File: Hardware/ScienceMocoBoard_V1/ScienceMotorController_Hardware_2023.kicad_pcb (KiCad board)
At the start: 2 copper layers, 153 x 106.4 mm, 189 parts, among them J1 RJ45_LED_Shielded, J2 Conn_02x03_Counter_Clockwise, Q1 SI4156DY, Q10 SI4156DY, Q11 SI4156DY, Q12 SI4156DY, Q13 SI4156DY, Q14 SI4156DY, Q15 SI4156DY, Q16 SI4156DY, Q2 SI4156DY, Q3 SI4156DY, Q4 SI4156DY, Q5 SI4156DY, Q6 SI4156DY, Q7 SI4156DY, Q8 SI4156DY, Q9 SI4156DY, SW1 SW_Push, SW10 SW_Push, SW11 SW_DPDT_x2, SW2 SW_Push, SW3 SW_Push, SW4 SW_Push, SW5 SW_Push, SW6 SW_Push, SW7 SW_Push, SW8 SW_Push, SW9 SW_Push, U1 74LVC2G04, U10 IRS2005S, U11 Teensy4.1_DEV-16771, U12 74LVC2G04, U13 IRS2005S, U14 IRS2005S, U15 IRS2005S, U2 IRS2005S, U3 3V3 OKI, U4 TSR_1-2450, U5 74LVC2G04, U6 IRS2005S, U7 IRS2005S, U8 IRS2005S, U9 74LVC2G04

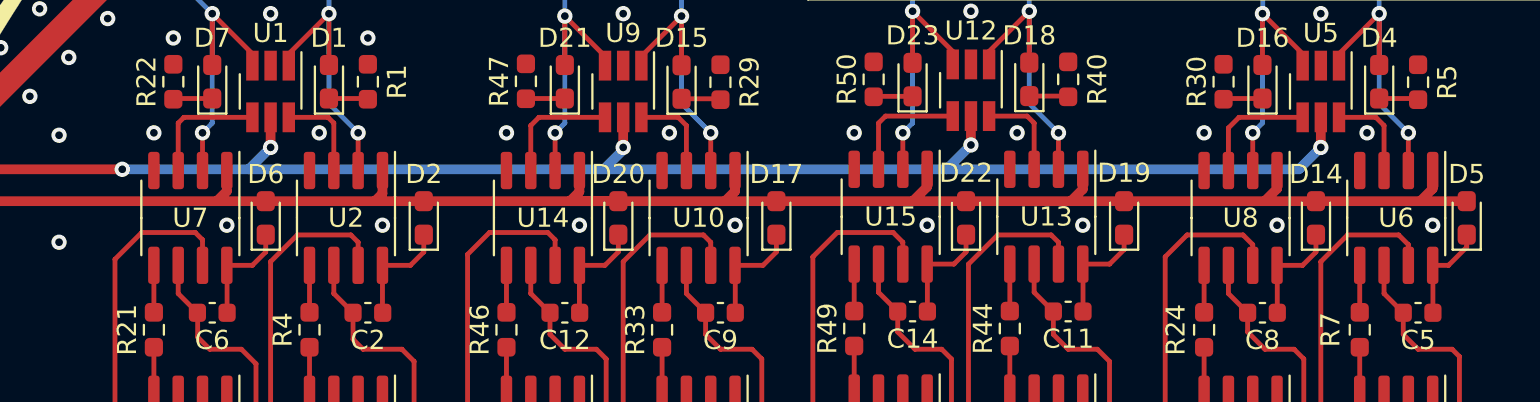
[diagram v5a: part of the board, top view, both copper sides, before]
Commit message: Fixed trace + made STEP file
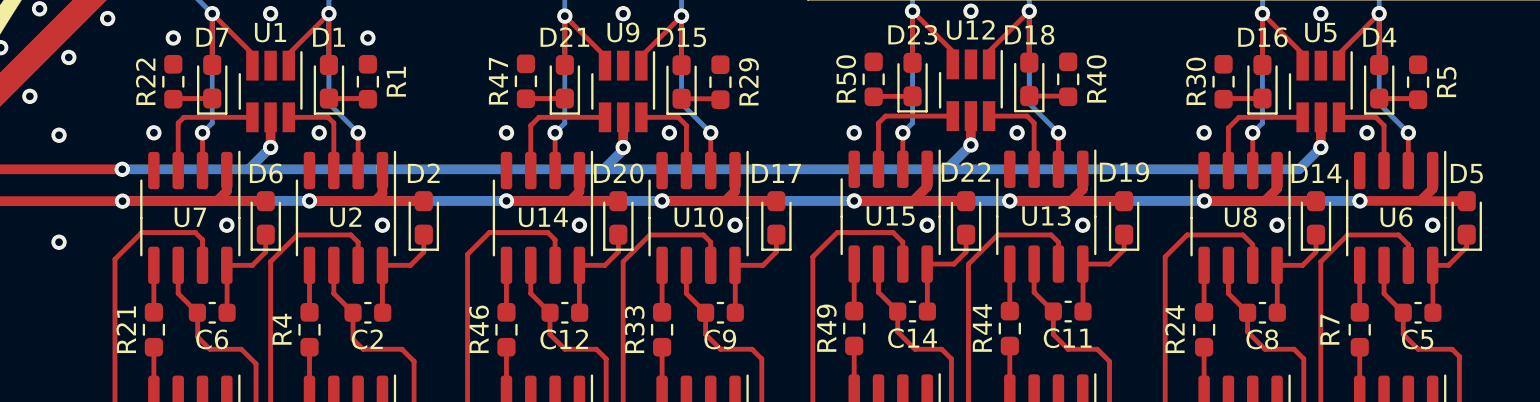
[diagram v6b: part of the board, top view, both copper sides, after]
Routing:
- net +12V: track 137.6 -> 178.1 mm, vias 69 -> 77
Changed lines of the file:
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@@
   (segment (start 123.4955 71.88) (end 66.294 71.88) (width 0.254) (layer "F.Cu") (net 6))
   (segment (start 64.90875 75.81795) (end 64.90875 78.7558) (width 0.254) (layer "F.Cu") (net 6))
+  (segment (start 145.175 117.235) (end 145.161 117.221) (width 0.508) (layer "F.Cu") (net 7))
+  (segment (start 130.288 117.235) (end 127.014 117.235) (width 0.508) (layer "F.Cu") (net 7))
   (segment (start 159.118 115.635) (end 159.118 116.586) (width 0.508) (layer "F.Cu") (net 7))
-  (segment (start 124.714 117.235) (end 130.288 117.235) (width 0.508) (layer "F.Cu") (net 7))
+  (segment (start 127.014 117.235) (end 127 117.221) (width 0.508) (layer "F.Cu") (net 7))
+  (segment (start 140.095 117.235) (end 137.047 117.235) (width 0.508) (layer "F.Cu") (net 7))
+  (segment (start 88.505 117.235) (end 84.328 121.412) (width 0.508) (layer "F.Cu") (net 7))
+  (segment (start 148.35 117.235) (end 145.175 117.235) (width 0.508) (layer "F.Cu") (net 7))
   (segment (start 148.971 115.57) (end 148.971 116.614) (width 0.508) (layer "F.Cu") (net 7))
   (segment (start 112.395 115.635) (end 112.395 116.84) (width 0.508) (layer "F.Cu") (net 7))
   (segment (start 42.6865 111.01575) (end 48.38375 116.713) (width 0.254) (layer "F.Cu") (net 7))
   (segment (start 158.469 117.235) (end 161.15 117.235) (width 0.508) (layer "F.Cu") (net 7))
-  (segment (start 151.13 117.235) (end 158.469 117.235) (width 0.508) (layer "F.Cu") (net 7))
-  (segment (start 84.328 121.412) (end 84.328 136.4628) (width 0.508) (layer "F.Cu") (net 7))
-  (segment (start 103.745 117.235) (end 88.505 117.235) (width 0.508) (layer "F.Cu") (net 7))
-  (segment (start 88.505 117.235) (end 84.328 121.412) (width 0.508) (layer "F.Cu") (net 7))
+  (segment (start 122.188 117.235) (end 118.886 117.235) (width 0.508) (layer "F.Cu") (net 7))
   (segment (start 48.387 123.19) (end 48.387 127.508) (width 0.254) (layer "F.Cu") (net 7))
   (segment (start 166.597 117.235) (end 169.024 117.235) (width 0.508) (layer "F.Cu") (net 7))
+  (segment (start 158.455 117.221) (end 158.469 117.235) (width 0.508) (layer "F.Cu") (net 7))
   (segment (start 104.267 116.713) (end 103.745 117.235) (width 0.508) (layer "F.Cu") (net 7))
   (segment (start 42.6865 111.01575) (end 42.6865 111.001) (width 0.254) (layer "F.Cu") (net 7))
+  (segment (start 84.328 121.412) (end 84.328 136.4628) (width 0.508) (layer "F.Cu") (net 7))
   (segment (start 159.118 116.586) (end 158.469 117.235) (width 0.508) (layer "F.Cu") (net 7))
   (segment (start 148.971 116.614) (end 148.35 117.235) (width 0.508) (layer "F.Cu") (net 7))
+  (segment (start 103.745 117.235) (end 88.505 117.235) (width 0.508) (layer "F.Cu") (net 7))
   (segment (start 140.843 115.57) (end 140.843 116.487) (width 0.508) (layer "F.Cu") (net 7))
   (segment (start 122.682 116.741) (end 122.188 117.235) (width 0.508) (layer "F.Cu") (net 7))
+  (segment (start 155.321 117.221) (end 158.455 117.221) (width 0.508) (layer "F.Cu") (net 7))
   (segment (start 140.095 117.235) (end 142.875 117.235) (width 0.508) (layer "F.Cu") (net 7))
-  (segment (start 142.875 117.235) (end 148.35 117.235) (width 0.508) (layer "F.Cu") (net 7))
+  (segment (start 112 117.235) (end 111.986 117.221) (width 0.508) (layer "F.Cu") (net 7))
   (segment (start 167.246 115.635) (end 167.246 116.586) (width 0.508) (layer "F.Cu") (net 7))
   (segment (start 167.246 116.586) (end 166.597 117.235) (width 0.508) (layer "F.Cu") (net 7))
-  (segment (start 132.969 117.235) (end 140.095 117.235) (width 0.508) (layer "F.Cu") (net 7))
-  (segment (start 114.554 117.235) (end 124.601 117.235) (width 0.508) (layer "F.Cu") (net 7))
+  (segment (start 111.986 117.221) (end 108.585 117.221) (width 0.508) (layer "F.Cu") (net 7))
+  (segment (start 137.047 117.235) (end 137.033 117.221) (width 0.508) (layer "F.Cu") (net 7))
   (segment (start 130.288 117.235) (end 132.969 117.235) (width 0.508) (layer "F.Cu") (net 7))
+  (segment (start 166.583 117.221) (end 166.597 117.235) (width 0.508) (layer "F.Cu") (net 7))
   (segment (start 112.395 116.84) (end 112 117.235) (width 0.508) (layer "F.Cu") (net 7))
   (segment (start 130.81 115.635) (end 130.81 116.713) (width 0.508) (layer "F.Cu") (net 7))
   (segment (start 48.38375 116.713) (end 48.387 116.713) (width 0.254) (layer "F.Cu") (net 7))
-  (segment (start 161.15 117.235) (end 166.597 117.235) (width 0.508) (layer "F.Cu") (net 7))
+  (segment (start 163.449 117.221) (end 166.583 117.221) (width 0.508) (layer "F.Cu") (net 7))
   (segment (start 130.81 116.713) (end 130.288 117.235) (width 0.508) (layer "F.Cu") (net 7))
-  (segment (start 106.299 117.235) (end 112 117.235) (width 0.508) (layer "F.Cu") (net 7))
   (segment (start 148.35 117.235) (end 151.13 117.235) (width 0.508) (layer "F.Cu") (net 7))
   (segment (start 103.745 117.235) (end 106.299 117.235) (width 0.508) (layer "F.Cu") (net 7))
@@
   (segment (start 112 117.235) (end 114.554 117.235) (width 0.508) (layer "F.Cu") (net 7))
   (segment (start 140.843 116.487) (end 140.095 117.235) (width 0.508) (layer "F.Cu") (net 7))
+  (segment (start 118.886 117.235) (end 118.872 117.221) (width 0.508) (layer "F.Cu") (net 7))
   (segment (start 122.682 115.635) (end 122.682 116.741) (width 0.508) (layer "F.Cu") (net 7))
   (segment (start 122.188 117.235) (end 124.714 117.235) (width 0.508) (layer "F.Cu") (net 7))
@@
   (via (at 143.002 148.336) (size 0.8) (drill 0.4) (layers "F.Cu" "B.Cu") (free) (net 7))
   (via (at 69.977 148.209) (size 0.8) (drill 0.4) (layers "F.Cu" "B.Cu") (free) (net 7))
+  (via (at 98.82 117.235) (size 0.8) (drill 0.4) (layers "F.Cu" "B.Cu") (net 7))
   (via (at 112.395 148.59) (size 0.8) (drill 0.4) (layers "F.Cu" "B.Cu") (free) (net 7))
   (via (at 161.29 148.336) (size 0.8) (drill 0.4) (layers "F.Cu" "B.Cu") (free) (net 7))
@@
   (via (at 111.125 148.59) (size 0.8) (drill 0.4) (layers "F.Cu" "B.Cu") (free) (net 7))
   (via (at 122.682 148.336) (size 0.8) (drill 0.4) (layers "F.Cu" "B.Cu") (free) (net 7))
+  (via (at 137.033 117.221) (size 0.8) (drill 0.4) (layers "F.Cu" "B.Cu") (net 7))
   (via (at 51.689 154.178) (size 0.8) (drill 0.4) (layers "F.Cu" "B.Cu") (free) (net 7))
   (via (at 143.002 156.464) (size 0.8) (drill 0.4) (layers "F.Cu" "B.Cu") (free) (net 7))
@@
   (via (at 104.267 148.59) (size 0.8) (drill 0.4) (layers "F.Cu" "B.Cu") (free) (net 7))
   (via (at 69.977 154.305) (size 0.8) (drill 0.4) (layers "F.Cu" "B.Cu") (free) (net 7))
+  (via (at 108.585 117.221) (size 0.8) (drill 0.4) (layers "F.Cu" "B.Cu") (net 7))
   (via (at 143.002 152.4) (size 0.8) (drill 0.4) (layers "F.Cu" "B.Cu") (free) (net 7))
   (via (at 164.706 148.463) (size 0.8) (drill 0.4) (layers "F.Cu" "B.Cu") (free) (net 7))
@@
   (via (at 124.714 148.336) (size 0.8) (drill 0.4) (layers "F.Cu" "B.Cu") (free) (net 7))
   (via (at 48.387 116.713) (size 0.8) (drill 0.4) (layers "F.Cu" "B.Cu") (net 7))
+  (via (at 155.321 117.221) (size 0.8) (drill 0.4) (layers "F.Cu" "B.Cu") (net 7))
   (via (at 143.002 154.432) (size 0.8) (drill 0.4) (layers "F.Cu" "B.Cu") (free) (net 7))
   (via (at 88.265 154.432) (size 0.8) (drill 0.4) (layers "F.Cu" "B.Cu") (free) (net 7))
@@
   (via (at 124.714 152.4) (size 0.8) (drill 0.4) (layers "F.Cu" "B.Cu") (free) (net 7))
   (via (at 109.855 148.59) (size 0.8) (drill 0.4) (layers "F.Cu" "B.Cu") (free) (net 7))
+  (via (at 163.449 117.221) (size 0.8) (drill 0.4) (layers "F.Cu" "B.Cu") (net 7))
   (via (at 101.727 148.59) (size 0.8) (drill 0.4) (layers "F.Cu" "B.Cu") (free) (net 7))
   (via (at 69.977 150.241) (size 0.8) (drill 0.4) (layers "F.Cu" "B.Cu") (free) (net 7))
@@
   (via (at 102.997 148.59) (size 0.8) (drill 0.4) (layers "F.Cu" "B.Cu") (free) (net 7))
   (via (at 129.54 148.336) (size 0.8) (drill 0.4) (layers "F.Cu" "B.Cu") (free) (net 7))
+  (via (at 118.872 117.221) (size 0.8) (drill 0.4) (layers "F.Cu" "B.Cu") (net 7))
   (via (at 140.843 148.463) (size 0.8) (drill 0.4) (layers "F.Cu" "B.Cu") (free) (net 7))
   (via (at 145.161 148.463) (size 0.8) (drill 0.4) (layers "F.Cu" "B.Cu") (free) (net 7))
   (via (at 88.265 156.464) (size 0.8) (drill 0.4) (layers "F.Cu" "B.Cu") (free) (net 7))
+  (via (at 127 117.221) (size 0.8) (drill 0.4) (layers "F.Cu" "B.Cu") (net 7))
   (via (at 69.977 156.337) (size 0.8) (drill 0.4) (layers "F.Cu" "B.Cu") (free) (net 7))
   (via (at 161.29 152.4) (size 0.8) (drill 0.4) (layers "F.Cu" "B.Cu") (free) (net 7))
@@
   (via (at 88.265 150.368) (size 0.8) (drill 0.4) (layers "F.Cu" "B.Cu") (free) (net 7))
   (via (at 106.426 152.654) (size 0.8) (drill 0.4) (layers "F.Cu" "B.Cu") (free) (net 7))
+  (via (at 145.161 117.221) (size 0.8) (drill 0.4) (layers "F.Cu" "B.Cu") (net 7))
   (via (at 51.689 148.082) (size 0.8) (drill 0.4) (layers "F.Cu" "B.Cu") (free) (net 7))
   (via (at 88.265 152.4) (size 0.8) (drill 0.4) (layers "F.Cu" "B.Cu") (free) (net 7))
   (via (at 157.848 148.463) (size 0.8) (drill 0.4) (layers "F.Cu" "B.Cu") (free) (net 7))
+  (segment (start 137.033 117.221) (end 145.161 117.221) (width 0.508) (layer "B.Cu") (net 7))
+  (segment (start 98.834 117.221) (end 108.585 117.221) (width 0.508) (layer "B.Cu") (net 7))
   (segment (start 48.387 116.713) (end 48.387 123.19) (width 0.254) (layer "B.Cu") (net 7))
+  (segment (start 155.321 117.221) (end 163.449 117.221) (width 0.508) (layer "B.Cu") (net 7))
+  (segment (start 98.82 117.235) (end 98.834 117.221) (width 0.508) (layer "B.Cu") (net 7))
+  (segment (start 127 117.221) (end 137.033 117.221) (width 0.508) (layer "B.Cu") (net 7))
+  (segment (start 145.161 117.221) (end 155.321 117.221) (width 0.508) (layer "B.Cu") (net 7))
+  (segment (start 118.872 117.221) (end 127 117.221) (width 0.508) (layer "B.Cu") (net 7))
+  (segment (start 108.585 117.221) (end 118.872 117.221) (width 0.508) (layer "B.Cu") (net 7))
   (segment (start 114.554 118.985) (end 114.554 119.888) (width 0.254) (layer "F.Cu") (net 8))
   (segment (start 112.395 120.585) (end 112.395 123.05) (width 0.254) (layer "F.Cu") (net 8))

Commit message: Worked on traces
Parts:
- D1, D15, D16, D18, D21, D23, D4, D7: value Pink -> Orange
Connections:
- U11 pad 11: Servo_4 -> Servo_6
- U11 pad 13: Servo_6 -> Servo_4
- U11 pad 30: Servo_5_SW -> unconnected-(U11-Pad30)
- U11 pad 31: Servo_6_SW -> Servo_5_SW
- U11 pad 32: unconnected-(U11-Pad32) -> Servo_6_SW
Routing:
- net Servo_4: track 80.5 -> 101.2 mm
- net Servo_6: track 77.7 -> 58.6 mm, vias 1 -> 0
- net GND: track 0.05 -> 11.0 mm, vias 155 -> 148
- net +5V: track 224.4 -> 225.5 mm, vias 1 -> 2
- net Servo_5: track 71.1 -> 72.3 mm, vias 1 -> 0
- net Servo_6_SW: track 86.8 -> 85.7 mm
- net Servo_5_SW: track 96.7 -> 95.6 mm
- net FWD_PWM_4: track 37.3 -> 37.4 mm, vias 3 -> 2
- net +3V3: vias 7 -> 5
- net RVS_PWM_4: vias 3 -> 2
- net RVS_PWM_3: vias 3 -> 2
- net RVS_PWM_2: vias 3 -> 2
- net RVS_PWM_1: vias 3 -> 2
- net FWD_PWM_3: vias 3 -> 2
- net FWD_PWM_2: vias 3 -> 2
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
